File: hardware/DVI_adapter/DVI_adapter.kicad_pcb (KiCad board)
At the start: 4 copper layers, 34.6 x 28.4 mm, 60 parts, among them J1 DF12NB(3.0)-30DS-0.5V(51), J2 DF12NB(3.0)-30DS-0.5V(51), J3 FPC Cable connector 1x20, U1 TXS0102DQE, U2 HE9009M6R, U3 TFP410

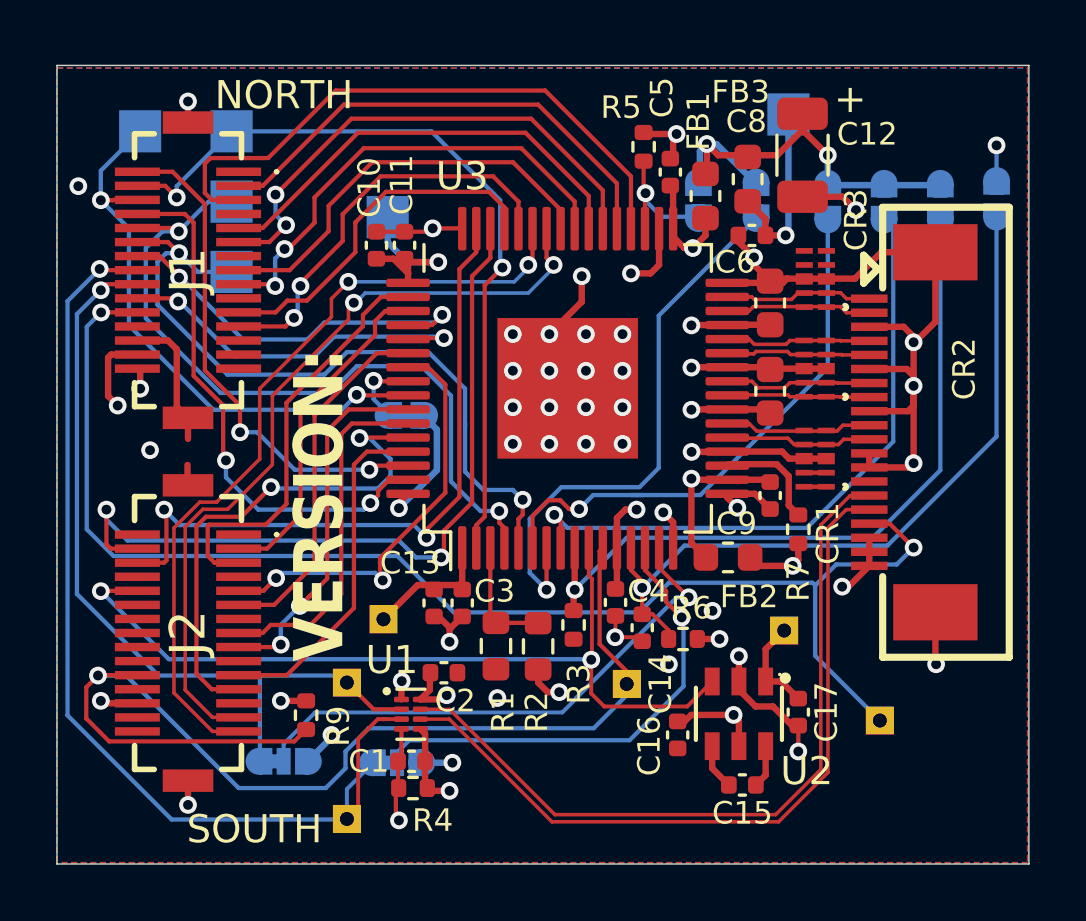
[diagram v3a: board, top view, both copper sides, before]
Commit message: review and update manufacturing constraints (via size, etc.)
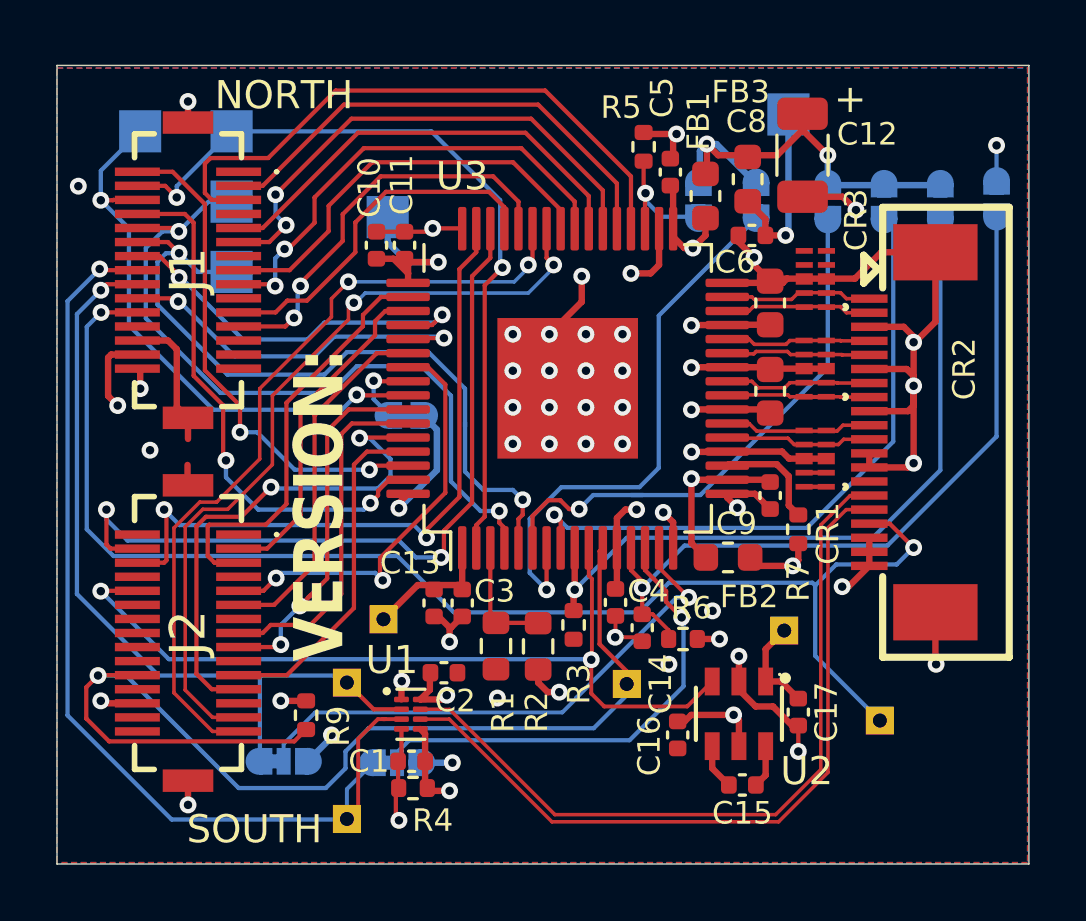
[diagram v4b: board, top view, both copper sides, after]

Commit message: change 20-pin FPC connector and update part numbers for manufacturing
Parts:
- J3: footprint Library:XFCN_F0501-B-20-20T-R -> easyeda2kicad:FPC-SMD_XUNPU_FPC-0.5FX-20PWBH15
- moved TP12 1.26 mm to (132.6, 135.0)
- moved J3 0.79 mm to (134.1, 126.0)
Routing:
- net HPD: track 49.1 -> 47.0 mm
- net GND: track 83.8 -> 81.9 mm, vias 47 -> 46
- net LCD_DE: track 28.1 -> 27.4 mm
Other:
- board text removed: "CERN OHL-S License"

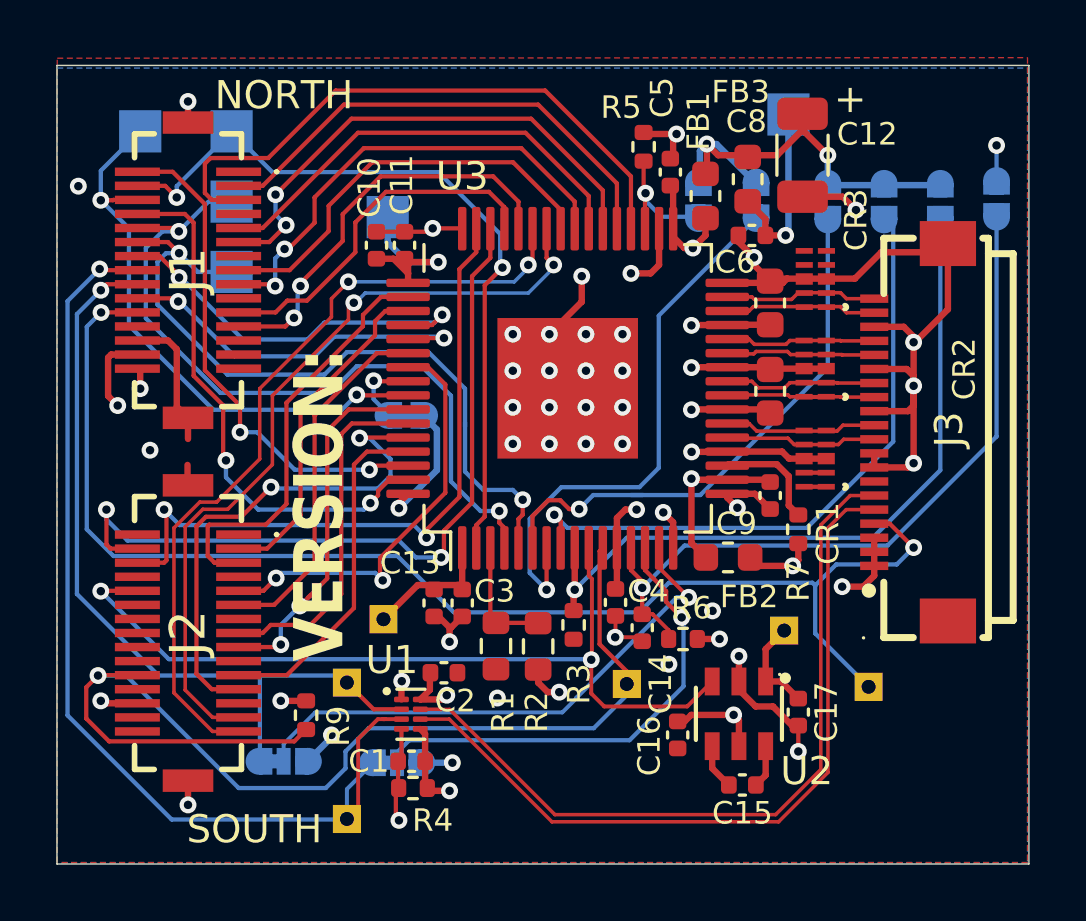
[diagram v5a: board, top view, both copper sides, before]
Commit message: fix R0/R1 mixup
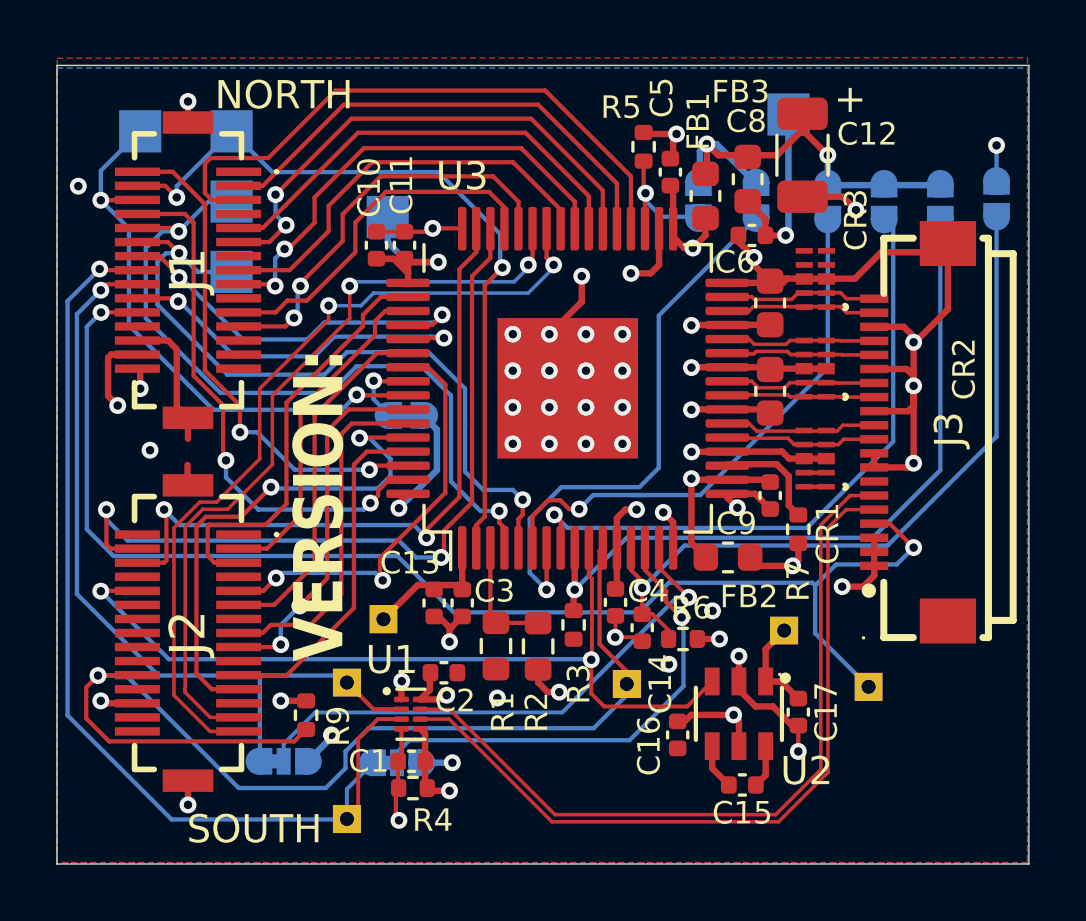
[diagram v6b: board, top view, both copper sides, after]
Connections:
- J2 pad 27: R1 -> R0
- J2 pad 29: R0 -> R1
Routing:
- net R1: track 27.9 -> 29.4 mm
- net R0: track 28.5 -> 27.8 mm
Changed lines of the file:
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@@
 			(size 0.3 1.6)
 			(layers "F.Cu" "F.Paste" "F.Mask")
-			(net 20 "R1")
+			(net 21 "R0")
 			(pinfunction "28")
 			(pintype "passive")
@@
 			(size 0.3 1.6)
 			(layers "F.Cu" "F.Paste" "F.Mask")
-			(net 21 "R0")
+			(net 20 "R1")
 			(pinfunction "30")
 			(pintype "passive")
@@
 	)
 	(segment
-		(start 109.8118 128.6882)
-		(end 108.926998 128.6882)
+		(start 107.9 135.3)
+		(end 109.1875 136.5875)
 		(width 0.127)
 		(layer "F.Cu")
@@
 	)
 	(segment
-		(start 108.3 129.315198)
-		(end 108.3 135.1145)
+		(start 109.4158 128.4342)
+		(end 108.8158 128.4342)
 		(width 0.127)
 		(layer "F.Cu")
@@
 	)
 	(segment
-		(start 109.273 136.0875)
-		(end 110.2 136.0875)
+		(start 108.8158 128.4342)
+		(end 107.9 129.35)
 		(width 0.127)
 		(layer "F.Cu")
@@
 	)
 	(segment
-		(start 121.4 120)
-		(end 121.15 119.75)
-		(width 0.1524)
+		(start 113.4 121.45)
+		(end 113.4 121.95)
+		(width 0.127)
 		(layer "F.Cu")
 		(net 20)
 	)
 	(segment
-		(start 121.15 119.75)
-		(end 121.15 118.7125)
-		(width 0.1524)
+		(start 107.9 129.35)
+		(end 107.9 135.3)
+		(width 0.127)
 		(layer "F.Cu")
 		(net 20)
 	)
 	(segment
-		(start 108.926998 128.6882)
-		(end 108.3 129.315198)
+		(start 113.4 121.95)
+		(end 110.95 124.4)
 		(width 0.127)
 		(layer "F.Cu")
@@
 	)
 	(segment
-		(start 114.105057 121.944943)
-		(end 111.4 124.65)
-		(width 0.127)
+		(start 121.4 120)
+		(end 121.15 119.75)
+		(width 0.1524)
 		(layer "F.Cu")
 		(net 20)
 	)
 	(segment
-		(start 111.4 124.65)
-		(end 111.4 127.1)
-		(width 0.127)
+		(start 121.15 119.75)
+		(end 121.15 118.7125)
+		(width 0.1524)
 		(layer "F.Cu")
 		(net 20)
 	)
 	(segment
-		(start 111.4 127.1)
-		(end 109.8118 128.6882)
+		(start 110.95 126.9)
+		(end 109.4158 128.4342)
 		(width 0.127)
 		(layer "F.Cu")
@@
 	)
 	(segment
-		(start 114.105057 121.519943)
-		(end 114.105057 121.944943)
+		(start 110.95 124.4)
+		(end 110.95 126.9)
 		(width 0.127)
 		(layer "F.Cu")
@@
 	)
 	(segment
-		(start 108.3 135.1145)
-		(end 109.273 136.0875)
+		(start 109.1875 136.5875)
+		(end 110.2 136.5875)
 		(width 0.127)
 		(layer "F.Cu")
@@
 	)
 	(via
-		(at 114.294943 121.344943)
+		(at 113.4 121.45)
 		(size 0.6)
 		(drill 0.3)
@@
 	)
 	(segment
-		(start 120.5 121)
-		(end 121.4 120.1)
+		(start 114.55 121.45)
+		(end 115 121)
 		(width 0.127)
 		(layer "B.Cu")
@@
 	)
 	(segment
-		(start 114.294943 121.344943)
-		(end 114.356771 121.344943)
+		(start 113.4 121.45)
+		(end 114.55 121.45)
 		(width 0.127)
 		(layer "B.Cu")
@@
 	)
 	(segment
-		(start 114.356771 121.344943)
-		(end 114.701714 121)
+		(start 120.5 121)
+		(end 121.4 120.1)
 		(width 0.127)
 		(layer "B.Cu")
@@
 	)
 	(segment
-		(start 114.701714 121)
+		(start 115 121)
 		(end 120.5 121)
 		(width 0.127)
@@
 	)
 	(segment
-		(start 107.9 129.35)
-		(end 108.8158 128.4342)
-		(width 0.127)
-		(layer "F.Cu")
-		(net 21)
-	)
-	(segment
 		(start 120.5 120)
 		(end 120.65 119.85)
@@
 	)
 	(segment
-		(start 109.273 136.5875)
-		(end 107.9 135.2145)
+		(start 108.3 135.05)
+		(end 108.3 135.1145)
 		(width 0.127)
 		(layer "F.Cu")
@@
 	)
 	(segment
-		(start 113.5 121.85)
-		(end 113.5 121.2)
+		(start 111.4 124.65)
+		(end 111.4 127.1)
 		(width 0.127)
 		(layer "F.Cu")
@@
 	)
 	(segment
-		(start 114.1 120.6)
-		(end 114.1 120.662501)
+		(start 108.3 135.05)
+		(end 108.3 135.2)
 		(width 0.127)
 		(layer "F.Cu")
@@
 	)
 	(segment
-		(start 108.8158 128.4342)
-		(end 109.4158 128.4342)
+		(start 111.4 127.1)
+		(end 109.8118 128.6882)
 		(width 0.127)
 		(layer "F.Cu")
@@
 	)
 	(segment
-		(start 110.95 124.4)
-		(end 113.5 121.85)
+		(start 114.15 121.9)
+		(end 111.4 124.65)
 		(width 0.127)
 		(layer "F.Cu")
@@
 	)
 	(segment
-		(start 120.65 119.85)
-		(end 120.65 118.7125)
-		(width 0.1524)
+		(start 108.926998 128.6882)
+		(end 108.3 129.315198)
+		(width 0.127)
 		(layer "F.Cu")
 		(net 21)
 	)
 	(segment
-		(start 113.5 121.2)
-		(end 114.1 120.6)
+		(start 108.3 135.2)
+		(end 109.1875 136.0875)
 		(width 0.127)
 		(layer "F.Cu")
@@
 	)
 	(segment
-		(start 109.4158 128.4342)
-		(end 110.95 126.9)
+		(start 120.65 119.85)
+		(end 120.65 118.7125)
+		(width 0.1524)
+		(layer "F.Cu")
+		(net 21)
+	)
+	(segment
+		(start 109.8118 128.6882)
+		(end 108.926998 128.6882)
 		(width 0.127)
 		(layer "F.Cu")
@@
 	)
 	(segment
-		(start 107.9 135.2145)
-		(end 107.9 129.35)
+		(start 109.1875 136.0875)
+		(end 110.2 136.0875)
 		(width 0.127)
 		(layer "F.Cu")
@@
 	)
 	(segment
-		(start 110.2 136.5875)
-		(end 109.273 136.5875)
+		(start 114.15 120.75)
+		(end 114.15 121.9)
 		(width 0.127)
 		(layer "F.Cu")
@@
 	)
 	(segment
-		(start 110.95 126.9)
-		(end 110.95 124.4)
+		(start 108.3 129.315198)
+		(end 108.3 135.05)
 		(width 0.127)
 		(layer "F.Cu")
@@
 	)
 	(via
-		(at 114.1 120.6)
+		(at 114.15 120.75)
 		(size 0.6)
 		(drill 0.3)
@@
 	)
 	(segment
+		(start 114.3 120.6)
+		(end 120 120.6)
+		(width 0.127)
+		(layer "B.Cu")
+		(net 21)
+	)
+	(segment
 		(start 120.5 120.1)
 		(end 120.5 120)
@@
 	)
 	(segment
-		(start 114.1 120.6)
-		(end 120 120.6)
+		(start 114.15 120.75)
+		(end 114.3 120.6)
 		(width 0.127)
 		(layer "B.Cu")

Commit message: fixes for producion and notes
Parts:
- moved C6 0.26 mm to (129.4, 121.4)
- moved C7 0.26 mm to (129.4, 124.5)
- moved CR1 0.26 mm to (131.0, 126.9)
- moved CR2 0.26 mm to (131.0, 123.7)
- moved CR3 0.26 mm to (131.0, 120.5)
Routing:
- net /TX0-: track 6.05 -> 5.26 mm
- net TVDD: track 24.8 -> 25.4 mm
